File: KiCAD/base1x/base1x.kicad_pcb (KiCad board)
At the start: 4 copper layers, 62.2 x 110 mm, 39 parts, among them J1 Conn_02x05_Odd_Even, J2 GS3, J3 Conn_02x14_Counter_Clockwise, J4 GS3, J6 Conn_02x14_Counter_Clockwise, J7 Conn_02x06_Counter_Clockwise, J8 Conn_02x06_Counter_Clockwise, J9 Screw_Terminal_01x08, P3 CONN_01X02, P4 CONN_01X02, U1 ADS1115

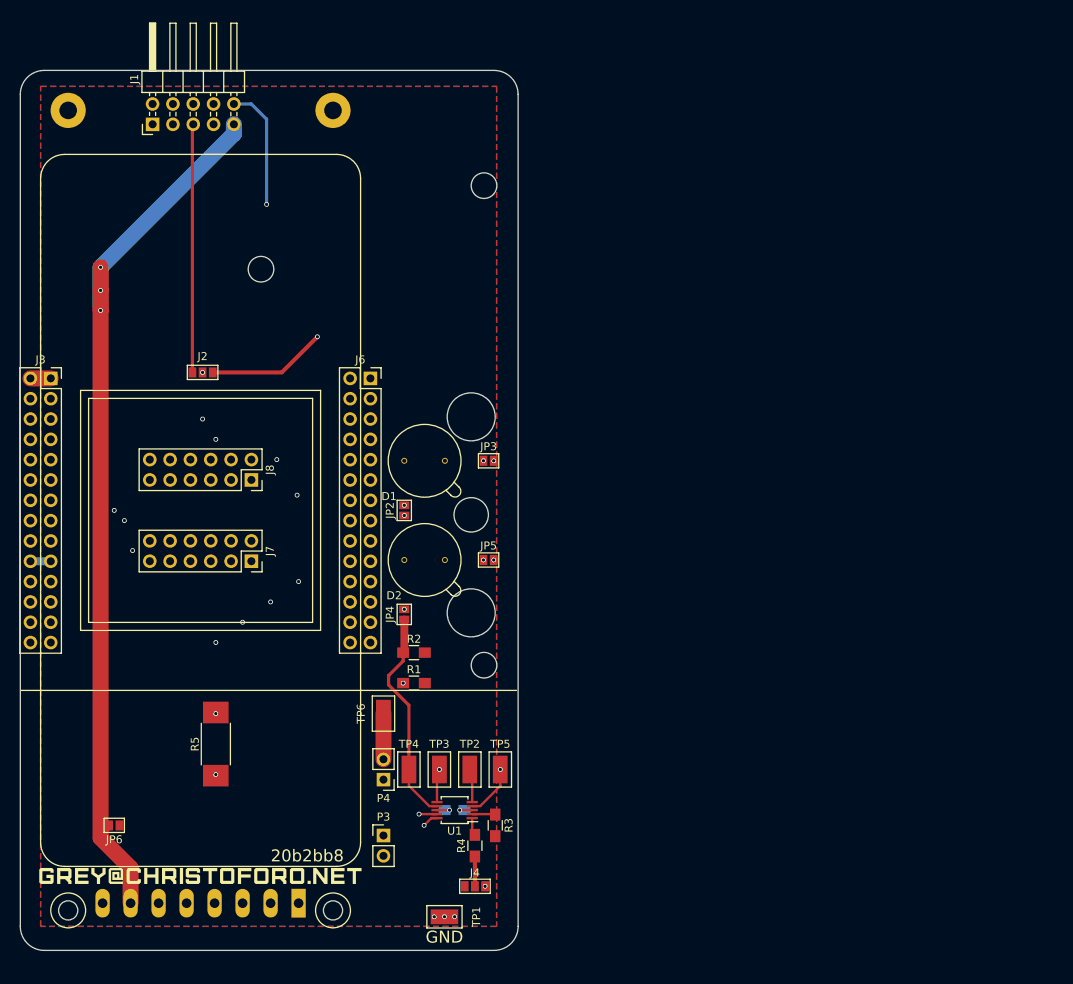
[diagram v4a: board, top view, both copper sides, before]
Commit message: upgrade syms and layouts to kicad5
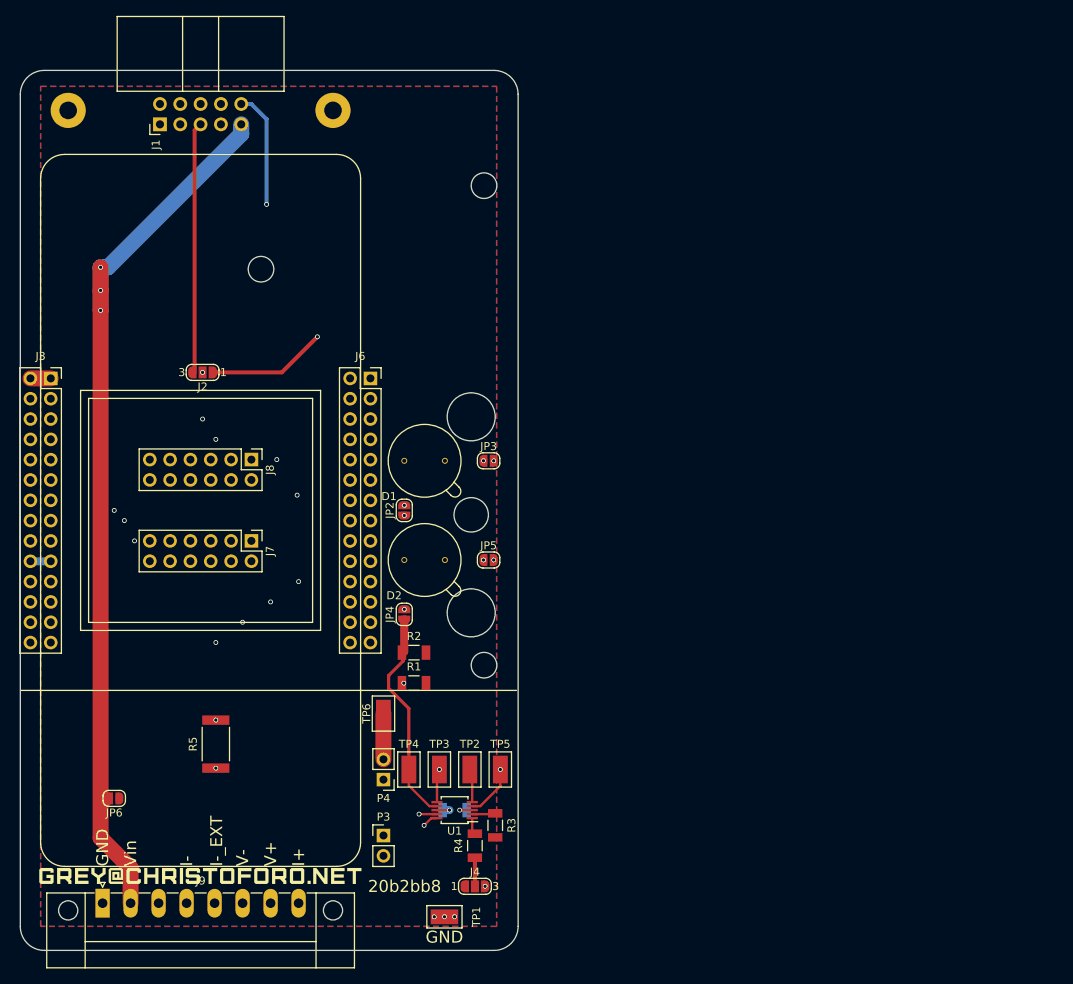
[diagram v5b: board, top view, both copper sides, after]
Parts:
- C1: footprint Capacitors_SMD:C_0805_HandSoldering -> Capacitor_SMD:C_1206_3216Metric
- J1: footprint Pin_Headers:Pin_Header_Angled_2x05_Pitch2.54mm -> Connector_IDC:IDC-Header_2x05_P2.54mm_Horizontal
- J2, J4: footprint Connectors:GS3 -> Jumper:SolderJumper-3_P1.3mm_Open_RoundedPad1.0x1.5mm_NumberLabels
- J3, J6: footprint Socket_Strips:Socket_Strip_Straight_2x14_Pitch2.54mm -> Connector_PinSocket_2.54mm:PinSocket_2x14_P2.54mm_Vertical
- J7, J8: footprint Socket_Strips:Socket_Strip_Straight_2x06_Pitch2.54mm -> Connector_PinHeader_2.54mm:PinHeader_2x06_P2.54mm_Vertical
- J9: footprint Connectors_Phoenix:PhoenixContact_MC-GF_08x3.50mm_Angled_ThreadedFlange_MountHole -> Connector_Phoenix_MC:PhoenixContact_MC_1,5_8-GF-3.5_1x08_P3.50mm_Horizontal_ThreadedFlange_MountHole; moved to F.Cu
- JP2, JP3, JP4, JP5, JP6: footprint Connectors:GS2 -> Jumper:SolderJumper-2_P1.3mm_Open_RoundedPad1.0x1.5mm
- MK1, MK2: footprint Mounting_Holes:MountingHole_2.2mm_M2_Pad -> MountingHole:MountingHole_2.2mm_M2_Pad
- MK3, MK4: footprint Mounting_Holes:MountingHole_6mm -> MountingHole:MountingHole_6mm
- MK5, MK7, MK8: footprint Mounting_Holes:MountingHole_3.2mm_M3 -> MountingHole:MountingHole_3.2mm_M3
- MK6: footprint Mounting_Holes:MountingHole_4.3mm_M4 -> MountingHole:MountingHole_4.3mm_M4
- P3, P4: footprint Pin_Headers:Pin_Header_Straight_1x02_Pitch2.54mm -> Connector_PinHeader_2.54mm:PinHeader_1x02_P2.54mm_Vertical
- R1, R2, R3, R4: footprint Resistors_SMD:R_0805_HandSoldering -> Resistor_SMD:R_1206_3216Metric
- R5: footprint Resistors_SMD:R_2512_HandSoldering -> Resistor_SMD:R_2512_6332Metric
- U1: footprint Housings_SSOP:MSOP-10_3x3mm_Pitch0.5mm -> Package_SO:MSOP-10_3x3mm_P0.5mm
- moved J9 24.5 mm to (-12.2, 49.1), turned to 0 degrees
- moved JP6 3.37 mm to (-10.8, 36.0), turned to 180 degrees
- moved J7 2.54 mm to (6.35, 3.81)
- moved J8 2.54 mm to (6.35, -6.35)
- moved J1 0.92 mm to (-5.08, -48.3)
- turned J2 to 180 degrees
- turned J4 to 0 degrees
- turned JP2 to 90 degrees
- turned JP3 to 0 degrees
- turned JP4 to 90 degrees
- turned JP5 to 0 degrees
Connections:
- J2 pad 1: V_D_EXT -> V_D_LOC
- J2 pad 3: V_D_LOC -> V_D_EXT
- J3 pad 12: /~CSL -> (no net)
- J3 pad 22: /I+L -> (no net)
- J3 pad 24: /V+L -> (no net)
- J3 pad 26: /V-L -> (no net)
- J3 pad 28: /I-L -> (no net)
- J4 pad 1: GND -> +5V
- J4 pad 3: +5V -> GND
- J6 pad 11: /~CSR -> (no net)
- J6 pad 21: /I+R -> (no net)
- J6 pad 23: /V+R -> (no net)
- J6 pad 25: /V-R -> (no net)
- J6 pad 27: /I-R -> (no net)
- J7 pad 1: Net-(J7-Pad1) -> (no net)
- J7 pad 10: Net-(J7-Pad10) -> (no net)
- J7 pad 11: Net-(J7-Pad11) -> (no net)
- J7 pad 12: Net-(J7-Pad12) -> (no net)
- J7 pad 2: Net-(J7-Pad2) -> (no net)
- J7 pad 3: Net-(J7-Pad3) -> (no net)
- J7 pad 4: Net-(J7-Pad4) -> (no net)
- J7 pad 5: Net-(J7-Pad5) -> (no net)
- J7 pad 6: Net-(J7-Pad6) -> (no net)
- J7 pad 7: Net-(J7-Pad7) -> (no net)
- J7 pad 8: Net-(J7-Pad8) -> (no net)
- J7 pad 9: Net-(J7-Pad9) -> (no net)
- J8 pad 1: Net-(J8-Pad1) -> (no net)
- J8 pad 10: Net-(J8-Pad10) -> (no net)
- J8 pad 11: Net-(J8-Pad11) -> (no net)
- J8 pad 12: Net-(J8-Pad12) -> (no net)
- J8 pad 2: Net-(J8-Pad2) -> (no net)
- J8 pad 3: Net-(J8-Pad3) -> (no net)
- J8 pad 4: Net-(J8-Pad4) -> (no net)
- J8 pad 5: Net-(J8-Pad5) -> (no net)
- J8 pad 6: Net-(J8-Pad6) -> (no net)
- J8 pad 7: Net-(J8-Pad7) -> (no net)
- J8 pad 8: Net-(J8-Pad8) -> (no net)
- J8 pad 9: Net-(J8-Pad9) -> (no net)
- J9 pad 1: I+ -> GND
- J9 pad 2: V+ -> /Vin
- J9 pad 3: V- -> (no net)
- J9 pad 4: I-_EXT -> I-
- J9 pad 5: I- -> I-_EXT
- J9 pad 6: Net-(J9-Pad6) -> V-
- J9 pad 7: /Vin -> V+
- J9 pad 8: GND -> I+
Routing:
- net SCK: track 98.9 -> 104.3 mm
- net /Vin: track 113.2 -> 118.1 mm
- net I+: track 77.6 -> 78.9 mm
- net I-_EXT: track 44.3 -> 45.5 mm
- net MOSI: track 97.1 -> 98.1 mm
- net MISO: track 94.4 -> 95.3 mm
- net ~CS0: track 92.4 -> 91.5 mm
- net +5V: track 4.10 -> 4.97 mm
- net I-: track 93.6 -> 94.4 mm
- net V+: track 75.1 -> 75.8 mm
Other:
- board text added: "+5V"
- board text added: "I+"
- board text added: "I-"
- board text added: "I-_EXT"
- board text added: "MISO"
- board text added: "MOSI"
- board text added: "SCK"
- board text added: "SCL"
- board text added: "SDA"
- board text added: "V+"
- board text added: "V-"
- board text added: "V_D_EXT"
- board text added: "Vin"
- board text added: "~CS0"

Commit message: update kicad and add logos
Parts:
- L1: footprint myParts:logo -> logo:logo_and_text
- moved L1 87.2 mm to (26.0, -37.5), turned to 90 degrees

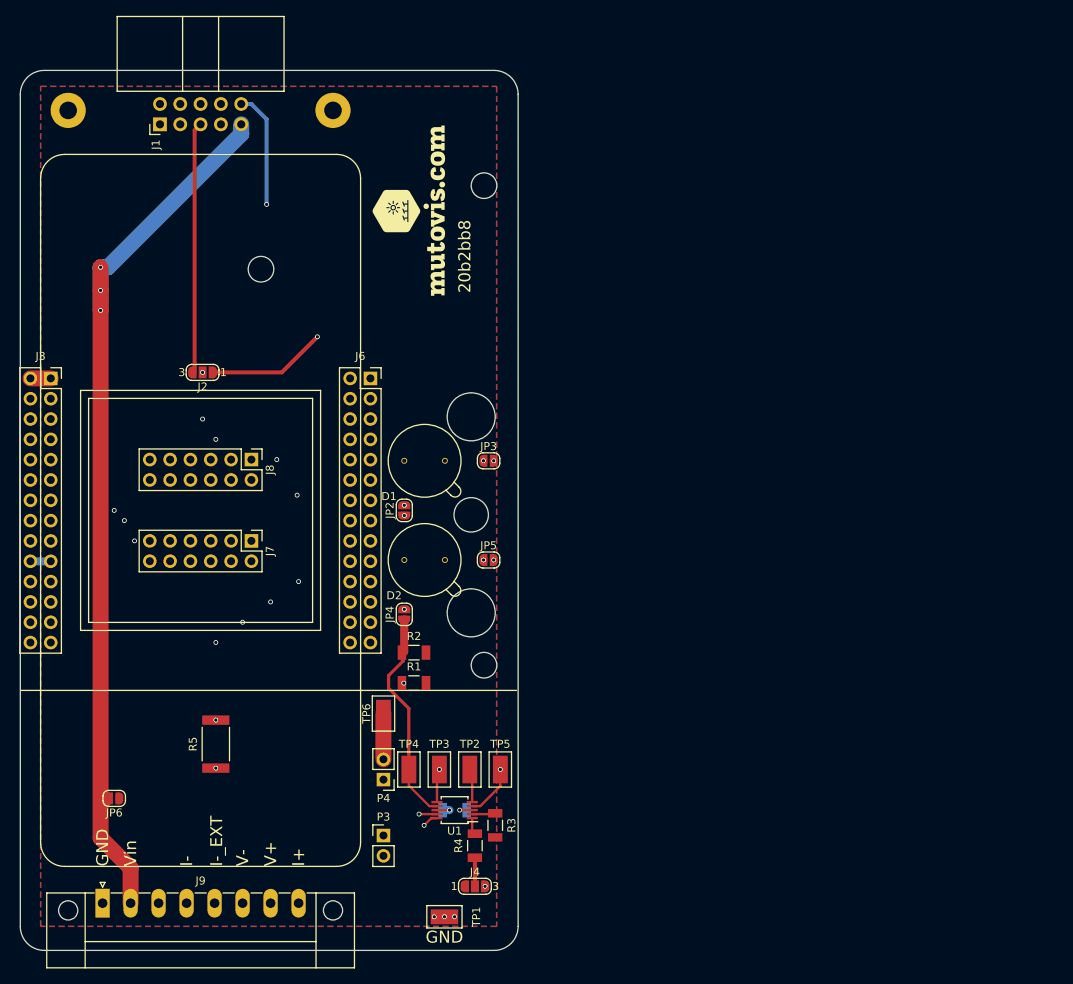
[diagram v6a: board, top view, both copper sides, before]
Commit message: new base1x layed out, mux updated and re-layed out
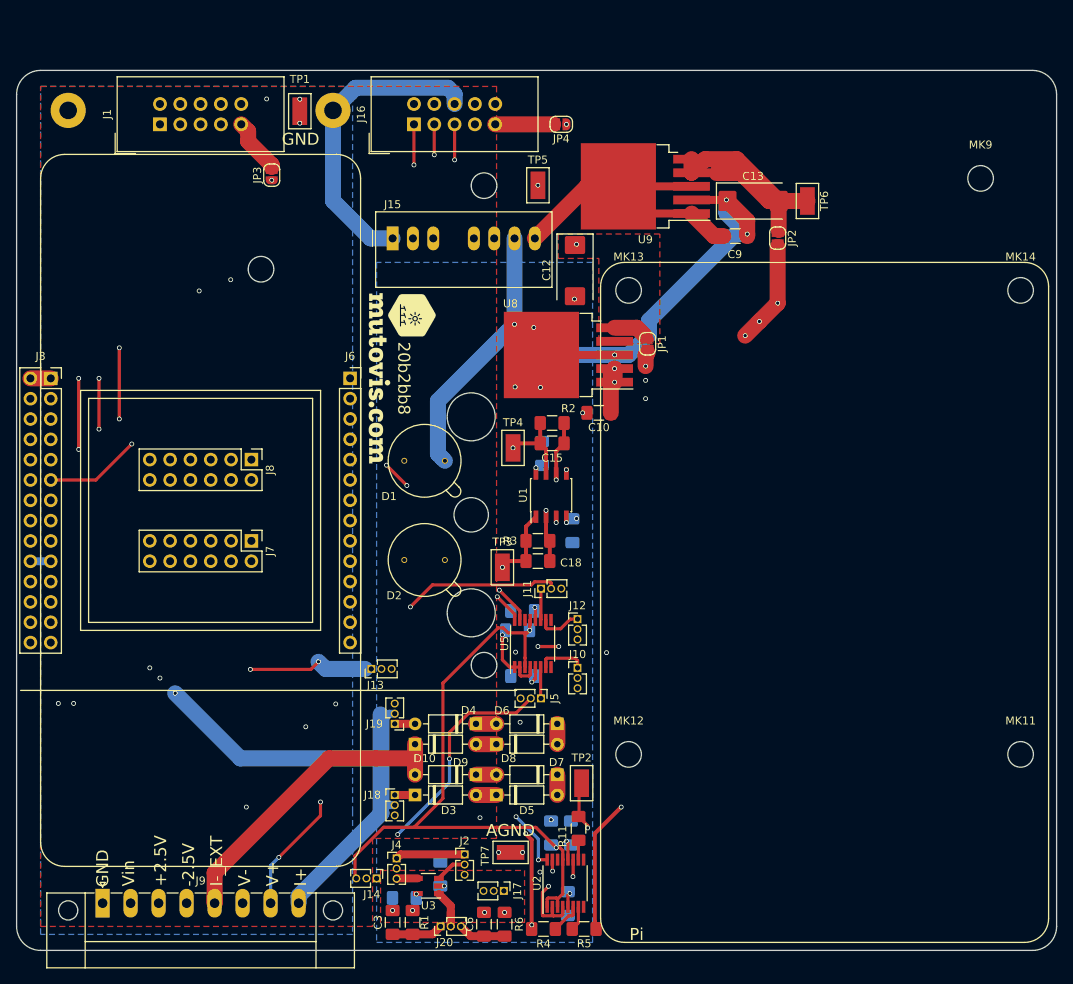
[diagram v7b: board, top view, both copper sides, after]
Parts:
- removed JP5, JP6: Jumper_NO_Small, Jumper:SolderJumper-2_P1.3mm_Open_RoundedPad1.0x1.5mm
- removed P3, P4: CONN_01X02, Connector_PinHeader_2.54mm:PinHeader_1x02_P2.54mm_Vertical
- added C10: 10uF, Capacitor_SMD:C_1206_3216Metric_Pad1.42x1.75mm_HandSolder, F.Cu at (49.8, -12.2)
- added C11: 0.1uF, Capacitor_SMD:C_1206_3216Metric_Pad1.42x1.75mm_HandSolder, B.Cu at (40.3, 20.7)
- added C12: 47uF, Capacitor_Tantalum_SMD:CP_EIA-7343-43_Kemet-X_Pad2.25x2.55mm_HandSolder, F.Cu at (46.8, -30.0)
- added C13: 47uF, Capacitor_Tantalum_SMD:CP_EIA-7343-43_Kemet-X_Pad2.25x2.55mm_HandSolder, F.Cu at (69.1, -38.7)
- added C14: 0.1uF, Capacitor_SMD:C_1206_3216Metric_Pad1.42x1.75mm_HandSolder, B.Cu at (39.6, 15.0)
- added C15: 0.1uF, Capacitor_SMD:C_1206_3216Metric_Pad1.42x1.75mm_HandSolder, F.Cu at (43.9, -8.38)
- added C16: 0.1uF, Capacitor_SMD:C_1206_3216Metric_Pad1.42x1.75mm_HandSolder, B.Cu at (42.7, -7.11)
- added C17: 0.1uF, Capacitor_SMD:C_1206_3216Metric_Pad1.42x1.75mm_HandSolder, B.Cu at (46.5, 2.54)
- added C18: 0.1uF, Capacitor_SMD:C_1206_3216Metric_Pad1.42x1.75mm_HandSolder, F.Cu at (42.2, 6.33)
- added C2: 0.1uF, Capacitor_SMD:C_1206_3216Metric_Pad1.42x1.75mm_HandSolder, B.Cu at (45.9, 49.1)
- added C3: 0.1uF, Capacitor_SMD:C_1206_3216Metric_Pad1.42x1.75mm_HandSolder, F.Cu at (24.0, 51.5)
- added C4: 0.1uF, Capacitor_SMD:C_1206_3216Metric_Pad1.42x1.75mm_HandSolder, B.Cu at (25.5, 48.5)
- added C5: 0.1uF, Capacitor_SMD:C_1206_3216Metric_Pad1.42x1.75mm_HandSolder, B.Cu at (30.0, 45.5)
- added C6: 0.1uF, Capacitor_SMD:C_1206_3216Metric_Pad1.42x1.75mm_HandSolder, F.Cu at (35.4, 51.7)
- added C7: 0.1uF, Capacitor_SMD:C_1206_3216Metric_Pad1.42x1.75mm_HandSolder, B.Cu at (43.8, 40.3)
- added C8: 0.1uF, Capacitor_SMD:C_1206_3216Metric_Pad1.42x1.75mm_HandSolder, B.Cu at (40.3, 12.6)
- added C9: 10uF, Capacitor_SMD:C_1206_3216Metric_Pad1.42x1.75mm_HandSolder, F.Cu at (66.8, -34.3)
- added D10: FDH333, Diode_THT:D_DO-35_SOD27_P7.62mm_Horizontal, F.Cu at (26.8, 29.2)
- added D3: FDH333, Diode_THT:D_DO-35_SOD27_P7.62mm_Horizontal, F.Cu at (26.8, 35.6)
- added D4: FDH333, Diode_THT:D_DO-35_SOD27_P7.62mm_Horizontal, F.Cu at (34.4, 26.7)
- added D5: FDH333, Diode_THT:D_DO-35_SOD27_P7.62mm_Horizontal, F.Cu at (37.0, 35.6)
- added D6: FDH333, Diode_THT:D_DO-35_SOD27_P7.62mm_Horizontal, F.Cu at (44.6, 26.7)
- added D7: FDH333, Diode_THT:D_DO-35_SOD27_P7.62mm_Horizontal, F.Cu at (44.6, 33.0)
- added D8: FDH333, Diode_THT:D_DO-35_SOD27_P7.62mm_Horizontal, F.Cu at (37.0, 29.2)
- added D9: FDH333, Diode_THT:D_DO-35_SOD27_P7.62mm_Horizontal, F.Cu at (34.4, 33.0)
- added J10: Conn_01x03, Connector_PinHeader_1.27mm:PinHeader_1x03_P1.27mm_Vertical, F.Cu at (47.1, 19.7)
- added J11: Conn_01x03, Connector_PinHeader_1.27mm:PinHeader_1x03_P1.27mm_Vertical, F.Cu at (42.5, 9.78)
- added J12: Conn_01x03, Connector_PinHeader_1.27mm:PinHeader_1x03_P1.27mm_Vertical, F.Cu at (47.1, 13.6)
- added J13: Conn_01x03, Connector_PinHeader_1.27mm:PinHeader_1x03_P1.27mm_Vertical, F.Cu at (21.3, 19.8)
- added J14: Conn_01x03, Connector_PinHeader_1.27mm:PinHeader_1x03_P1.27mm_Vertical, F.Cu at (22.0, 46.0)
- added J15: Conn_01x08, Converter_DCDC:Converter_DCDC_TRACO_TMR-xxxx_THT, F.Cu at (24.0, -34.0)
- added J16: Conn_02x05_Odd_Even, Connector_IDC:IDC-Header_2x05_P2.54mm_Vertical, F.Cu at (26.7, -48.3)
- added J17: Conn_01x03, Connector_PinHeader_1.27mm:PinHeader_1x03_P1.27mm_Vertical, F.Cu at (37.9, 47.6)
- added J18: Conn_01x03, Connector_PinHeader_1.27mm:PinHeader_1x03_P1.27mm_Vertical, F.Cu at (24.3, 35.6)
- added J19: Conn_01x03, Connector_PinHeader_1.27mm:PinHeader_1x03_P1.27mm_Vertical, F.Cu at (24.3, 26.7)
- added J20: Conn_01x03, Connector_PinHeader_1.27mm:PinHeader_1x03_P1.27mm_Vertical, F.Cu at (30.0, 52.0)
- added J5: Conn_01x03, Connector_PinHeader_1.27mm:PinHeader_1x03_P1.27mm_Vertical, F.Cu at (42.5, 23.5)
- added JP1: Jumper_NC_Small, Jumper:SolderJumper-2_P1.3mm_Open_RoundedPad1.0x1.5mm, F.Cu at (55.9, -20.8)
- added MK11: Mounting_Hole, MountingHole:MountingHole_3.2mm_M3, F.Cu at (102.5, 30.5)
- added MK12: Mounting_Hole, MountingHole:MountingHole_3.2mm_M3, F.Cu at (53.5, 30.5)
- added MK13: Mounting_Hole, MountingHole:MountingHole_3.2mm_M3, F.Cu at (53.5, -27.5)
- added MK14: Mounting_Hole, MountingHole:MountingHole_3.2mm_M3, F.Cu at (102.5, -27.5)
- added MK9: Mounting_Hole, MountingHole:MountingHole_3.2mm_M3, F.Cu at (97.5, -41.5)
- added R11: 51R, Resistor_SMD:R_1206_3216Metric_Pad1.42x1.75mm_HandSolder, F.Cu at (47.2, 39.8)
- added R6: 1k, Resistor_SMD:R_1206_3216Metric_Pad1.42x1.75mm_HandSolder, F.Cu at (38.0, 51.7)
- added TP7: Test_Point, myParts:Test_Point_S1751-46R, F.Cu at (38.8, 42.8)
- added U2: ads122c04, Package_SO:TSSOP-16_4.4x5mm_P0.65mm, F.Cu at (45.6, 46.6)
- added U3: AD8615, Package_TO_SOT_SMD:TSOT-23-5, F.Cu at (28.5, 47.0)
- added U5: ads122c04, Package_SO:TSSOP-16_4.4x5mm_P0.65mm, F.Cu at (41.5, 16.6)
- added U8: LT1963EQ-2.5, Package_TO_SOT_SMD:TO-263-5_TabPin3, F.Cu at (46.0, -19.4)
- added U9: LT3015EQ-2.5, Package_TO_SOT_SMD:TO-263-5_TabPin3, F.Cu at (55.6, -40.5)
- added logo: G***, logo:logo, F.Cu at (26.4, -24.4)
- C1: value 1uF -> 0.1uF; footprint Capacitor_SMD:C_1206_3216Metric -> Capacitor_SMD:C_1206_3216Metric_Pad1.42x1.75mm_HandSolder
- J1: footprint Connector_IDC:IDC-Header_2x05_P2.54mm_Horizontal -> Connector_IDC:IDC-Header_2x05_P2.54mm_Vertical
- J2, J4: value GS3 -> Conn_01x03; footprint Jumper:SolderJumper-3_P1.3mm_Open_RoundedPad1.0x1.5mm_NumberLabels -> Connector_PinHeader_1.27mm:PinHeader_1x03_P1.27mm_Vertical
- J6: value Conn_02x14_Counter_Clockwise -> Conn_01x14_Counter_Clockwise; footprint Connector_PinSocket_2.54mm:PinSocket_2x14_P2.54mm_Vertical -> Connector_PinSocket_2.54mm:PinSocket_1x14_P2.54mm_Vertical
- JP2: value Jumper_NO_Small -> Jumper_NC_Small
- L1: value GREY@CHRISTOFORO.NET -> grey@mutovis.com; footprint logo:logo_and_text -> logo:text
- R1: value 1.2K -> 20R; footprint Resistor_SMD:R_1206_3216Metric -> Resistor_SMD:R_1206_3216Metric_Pad1.42x1.75mm_HandSolder
- R2: value 1.2K -> 1k; footprint Resistor_SMD:R_1206_3216Metric -> Resistor_SMD:R_1206_3216Metric_Pad1.42x1.75mm_HandSolder
- R3: value 10K -> 1k; footprint Resistor_SMD:R_1206_3216Metric -> Resistor_SMD:R_1206_3216Metric_Pad1.42x1.75mm_HandSolder
- R4: value 10K -> 51R; footprint Resistor_SMD:R_1206_3216Metric -> Resistor_SMD:R_1206_3216Metric_Pad1.42x1.75mm_HandSolder
- R5: value 1 -> 51R; footprint Resistor_SMD:R_2512_6332Metric -> Resistor_SMD:R_1206_3216Metric_Pad1.42x1.75mm_HandSolder
- U1: value ADS1115 -> AD8616; footprint Package_SO:MSOP-10_3x3mm_P0.5mm -> Package_SO:SOIC-8_3.9x4.9mm_P1.27mm
- moved TP1 102.3 mm to (12.4, -49.9), turned to 270 degrees
- moved TP6 83.2 mm to (75.9, -38.7), turned to 270 degrees
- moved TP5 73.2 mm to (42.2, -40.6)
- moved J2 68.6 mm to (33.0, 43.0), turned to 0 degrees
- moved JP4 64.3 mm to (45.1, -48.3), turned to 180 degrees
- moved JP2 57.8 mm to (72.1, -34.0), turned to 270 degrees
- moved R5 51.5 mm to (47.9, 52.3), turned to 180 degrees
- moved JP3 44.8 mm to (8.89, -41.9), turned to 90 degrees
- moved TP4 42.3 mm to (39.1, -7.81)
- moved U1 41.2 mm to (43.8, -1.91), turned to 90 degrees
- moved R3 36.0 mm to (42.2, 3.81), turned to 0 degrees
- moved R2 33.5 mm to (43.9, -10.9)
- moved R1 29.9 mm to (26.5, 51.5), turned to 90 degrees
- moved TP3 26.5 mm to (37.7, 7.11)
- moved L1 21.3 mm to (22.4, -16.5), turned to 270 degrees
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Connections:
- C1 pad 1: +5V -> +2V5
- C1 pad 2: GND -> GNDREF
- D1 pad 1: Net-(D1-Pad1) -> Net-(C18-Pad1)
- D1 pad 2: Net-(D1-Pad2) -> GNDREF
- D2 pad 1: Net-(D2-Pad1) -> Net-(C15-Pad1)
- D2 pad 2: Net-(D2-Pad2) -> GNDREF
- J1 pad 5: V_D_EXT -> /EnableTraco
- J1 pad 9: /Vin -> Net-(J1-Pad9)
- J2 pad 1: V_D_LOC -> I-_EXT
- J2 pad 2: V_D -> Net-(J2-Pad2)
- J2 pad 3: V_D_EXT -> GNDREF
- J3 pad 12: (no net) -> Net-(J3-Pad12)
- J3 pad 22: (no net) -> Net-(J3-Pad22)
- J3 pad 24: (no net) -> Net-(J3-Pad24)
- J3 pad 26: (no net) -> Net-(J3-Pad26)
- J3 pad 28: (no net) -> Net-(J3-Pad28)
- J4 pad 1: +5V -> I-_EXT
- J4 pad 2: Net-(J4-Pad2) -> I-
- J4 pad 3: GND -> Net-(C3-Pad2)
- J6 pad 1: +5V -> Net-(J6-Pad1)
- J6 pad 10: SCL -> Net-(J6-Pad10)
- J6 pad 11: (no net) -> Net-(J6-Pad11)
- J6 pad 12: ~CS0 -> Net-(J6-Pad12)
- J6 pad 13: MISO -> Net-(J6-Pad13)
- J6 pad 14: MISO -> Net-(J6-Pad14)
- J6 pad 2: +5V -> Net-(J6-Pad2)
- J6 pad 3: +3V3 -> Net-(J6-Pad3)
- J6 pad 4: +3V3 -> Net-(J6-Pad4)
- J6 pad 5: V_D -> Net-(J6-Pad5)
- J6 pad 6: V_D -> Net-(J6-Pad6)
- J6 pad 7: SDA -> Net-(J6-Pad7)
- J6 pad 8: SDA -> Net-(J6-Pad8)
- J6 pad 9: SCL -> Net-(J6-Pad9)
- J7 pad 1: (no net) -> Net-(J7-Pad1)
- J7 pad 10: (no net) -> Net-(J7-Pad10)
- J7 pad 11: (no net) -> Net-(J7-Pad11)
- J7 pad 12: (no net) -> Net-(J7-Pad12)
- J7 pad 2: (no net) -> Net-(J7-Pad2)
- J7 pad 3: (no net) -> Net-(J7-Pad3)
- J7 pad 4: (no net) -> Net-(J7-Pad4)
- J7 pad 5: (no net) -> Net-(J7-Pad5)
- J7 pad 6: (no net) -> Net-(J7-Pad6)
- J7 pad 7: (no net) -> Net-(J7-Pad7)
- J7 pad 8: (no net) -> Net-(J7-Pad8)
- J7 pad 9: (no net) -> Net-(J7-Pad9)
- J8 pad 1: (no net) -> Net-(J8-Pad1)
- J8 pad 10: (no net) -> Net-(J8-Pad10)
- J8 pad 11: (no net) -> Net-(J8-Pad11)
- J8 pad 12: (no net) -> Net-(J8-Pad12)
- J8 pad 2: (no net) -> Net-(J8-Pad2)
- J8 pad 3: (no net) -> Net-(J8-Pad3)
- J8 pad 4: (no net) -> Net-(J8-Pad4)
- J8 pad 5: (no net) -> Net-(J8-Pad5)
- J8 pad 6: (no net) -> Net-(J8-Pad6)
- J8 pad 7: (no net) -> Net-(J8-Pad7)
- J8 pad 8: (no net) -> Net-(J8-Pad8)
- J8 pad 9: (no net) -> Net-(J8-Pad9)
- J9 pad 3: (no net) -> +2V5
- J9 pad 4: I- -> -2V5
- JP2 pad 1: Net-(JP2-Pad1) -> Net-(C13-Pad2)
- JP2 pad 2: Net-(D1-Pad1) -> -2V5
- JP3 pad 1: Net-(D1-Pad2) -> /Vin
- JP3 pad 2: GND -> Net-(J1-Pad9)
- JP4 pad 1: Net-(JP4-Pad1) -> /Vin
- JP4 pad 2: Net-(D2-Pad1) -> Net-(J16-Pad9)
- MK3 pad 1: (no net) -> Net-(MK3-Pad1)
- MK4 pad 1: (no net) -> Net-(MK4-Pad1)
- MK5 pad 1: (no net) -> Net-(MK5-Pad1)
- MK6 pad 1: (no net) -> Net-(MK6-Pad1)
- MK7 pad 1: (no net) -> Net-(MK7-Pad1)
- MK8 pad 1: (no net) -> Net-(MK8-Pad1)
- R1 pad 1: Net-(JP2-Pad1) -> Net-(C3-Pad1)
- R1 pad 2: +5V -> Net-(C3-Pad2)
- R2 pad 1: Net-(JP4-Pad1) -> Net-(C15-Pad2)
- R2 pad 2: +5V -> Net-(C15-Pad1)
- R3 pad 1: Net-(R3-Pad1) -> Net-(C18-Pad2)
- R3 pad 2: +5V -> Net-(C18-Pad1)
- R4 pad 1: Net-(J4-Pad2) -> Net-(C15-Pad2)
- R4 pad 2: Net-(R4-Pad2) -> /V_D2
- R5 pad 1: I-_EXT -> Net-(C18-Pad2)
- R5 pad 2: I- -> /V_D1
- TP2 pad 1: Net-(TP2-Pad1) -> Net-(J20-Pad2)
- TP3 pad 1: Net-(JP2-Pad1) -> Net-(C18-Pad2)
- TP4 pad 1: Net-(JP4-Pad1) -> Net-(C15-Pad2)
- TP5 pad 1: V_D_LOC -> Net-(C12-Pad1)
- TP6 pad 1: I- -> Net-(C13-Pad2)
- U1 pad 1: Net-(R4-Pad2) -> Net-(C18-Pad2)
- U1 pad 2: Net-(R3-Pad1) -> Net-(C18-Pad1)
- U1 pad 3: GND -> GNDREF
- U1 pad 4: V_D_LOC -> -2V5
- U1 pad 5: Net-(TP2-Pad1) -> GNDREF
- U1 pad 6: Net-(JP2-Pad1) -> Net-(C15-Pad1)
- U1 pad 7: Net-(JP4-Pad1) -> Net-(C15-Pad2)
- U1 pad 8: +5V -> +2V5
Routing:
- net -2V5: track 0.00 -> 188.7 mm, vias 0 -> 9
- net +2V5: track 0.00 -> 186.0 mm, vias 0 -> 7
- net GND: track 4.11 -> 179.4 mm, vias 7 -> 8
- net GNDREF: track 0.00 -> 92.0 mm, vias 0 -> 13
- net V_D_LOC: track 90.7 -> 0.00 mm, vias 2 -> 0
- net +5V: track 4.97 -> 86.8 mm, vias 1 -> 2
- net Net-(C15-Pad2): track 0.00 -> 76.1 mm, vias 0 -> 3
- net Net-(C18-Pad2): track 0.00 -> 69.4 mm, vias 0 -> 2
- net V_D: track 48.3 -> 104.0 mm
- net /EnableTraco: track 0.00 -> 53.0 mm, vias 0 -> 2
- net SDA: track 133.7 -> 185.9 mm, vias 2 -> 7
- net SCL: track 142.4 -> 187.1 mm, vias 2 -> 4
- net I+: track 78.9 -> 120.8 mm, vias 1 -> 4
- net /Vin: track 118.1 -> 159.3 mm, vias 3 -> 2
- net +3V3: track 42.5 -> 2.54 mm
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- added copper zone on B.Cu, net GNDREF
- added copper zone on F.Cu, net Net-(C12-Pad1)
- added copper zone on F.Cu, net Net-(C3-Pad2)
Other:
- board size 62.2 x 110 mm -> 130 x 110 mm
- board text added: "+2.5V"
- board text added: "-2.5V"
- board text added: "AGND"
- board text added: "Pi"
- board text removed: "I-"
